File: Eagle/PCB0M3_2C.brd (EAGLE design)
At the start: 152.4 x 241.3 mm, 203 parts, among them J1 J_MC32857, J2 0399700102, J3 J_1546074-2282834-2, J4 J_1546074-2282834-2, J5 J_1546074-2282834-2, J6 J_1546074-2282834-2, J7 J_1546074-2282834-2, J8 J_1546074-2282834-2, Q1 U_FDPF045N10A_TO-220F, Q10 Q_2N7000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

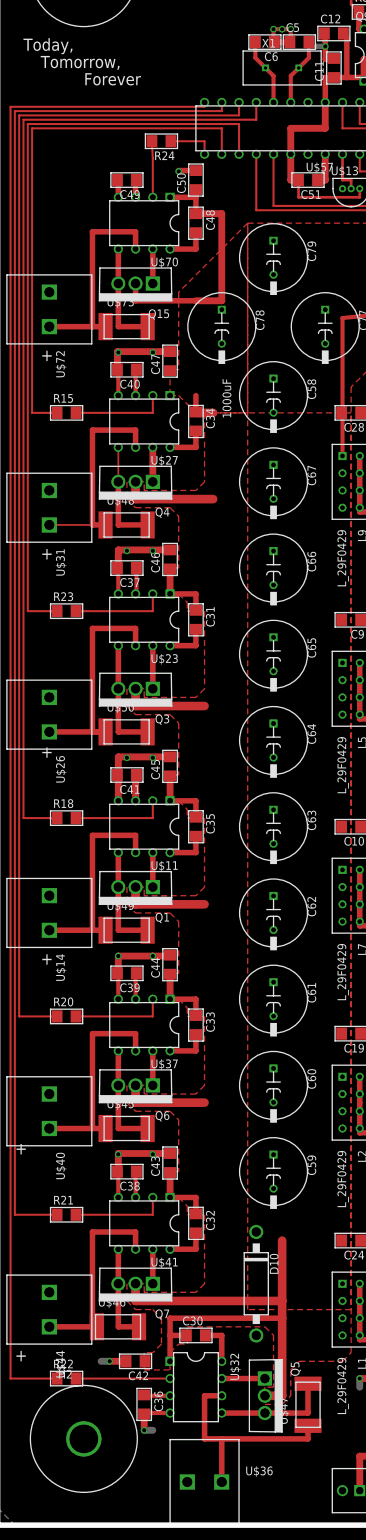
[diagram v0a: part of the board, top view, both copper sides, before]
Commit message: Power Board Cleanup and Trace Fixes
Fixed motor output traces to handle currents as well as removed thermals
from some parts for e-table.
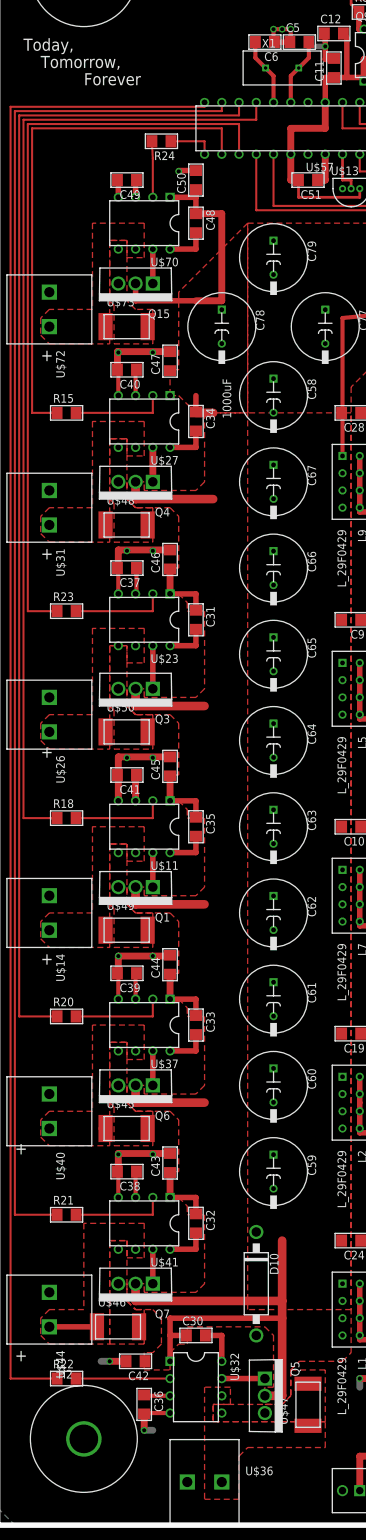
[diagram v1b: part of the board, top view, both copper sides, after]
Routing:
- net N$55: track 42.6 -> 0.00 mm
- net N$67: track 32.4 -> 0.00 mm
- net N$72: track 31.8 -> 0.66 mm
- net N$94: track 31.1 -> 0.00 mm
- net N$61: track 31.1 -> 0.00 mm
- net N$40: track 31.1 -> 0.00 mm
- net N$77: track 29.9 -> 7.01 mm
- net N$66: track 17.0 -> 0.00 mm
- net N$52: track 17.0 -> 0.00 mm
- net N$81: track 15.8 -> 0.00 mm
- net N$60: track 15.8 -> 0.00 mm
- net N$39: track 15.8 -> 0.00 mm
- net N$71: track 15.7 -> 0.00 mm
- net N$76: track 14.5 -> 0.00 mm
- added copper zone on layer 1, net N$39
- added copper zone on layer 1, net N$40
- added copper zone on layer 1, net N$52
- added copper zone on layer 1, net N$55
- added copper zone on layer 1, net N$60
- added copper zone on layer 1, net N$61
- added copper zone on layer 1, net N$66
- added copper zone on layer 1, net N$67
- added copper zone on layer 1, net N$71
- added copper zone on layer 1, net N$72
- added copper zone on layer 1, net N$76
- added copper zone on layer 1, net N$77
- added copper zone on layer 1, net N$81
- added copper zone on layer 1, net N$94
